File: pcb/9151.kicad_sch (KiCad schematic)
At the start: 22 parts, among them J1 SIM_Card, J10 Conn_01x02, J5 Conn_ARM_SWD_TagConnect_TC203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, J9 Conn_Coaxial, U1 nRF9151-LAXX, U3 W25Q128JVP

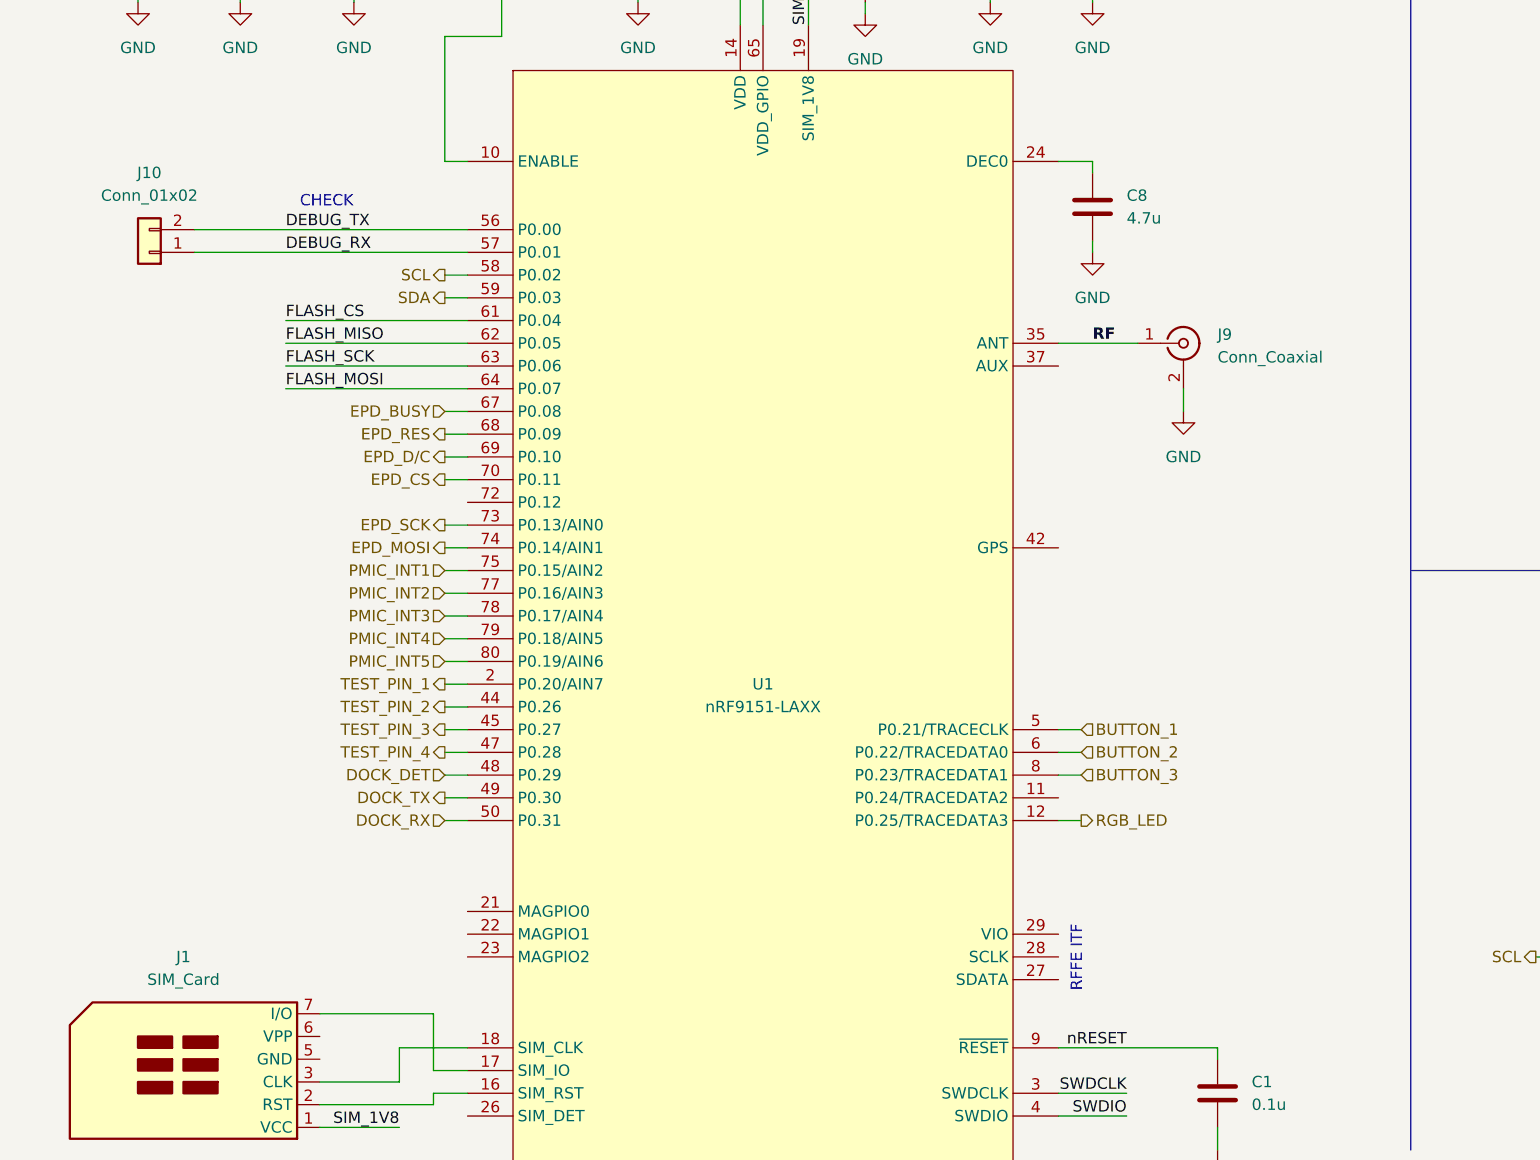
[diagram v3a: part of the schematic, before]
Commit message: Add netclasses and usb-to-uart
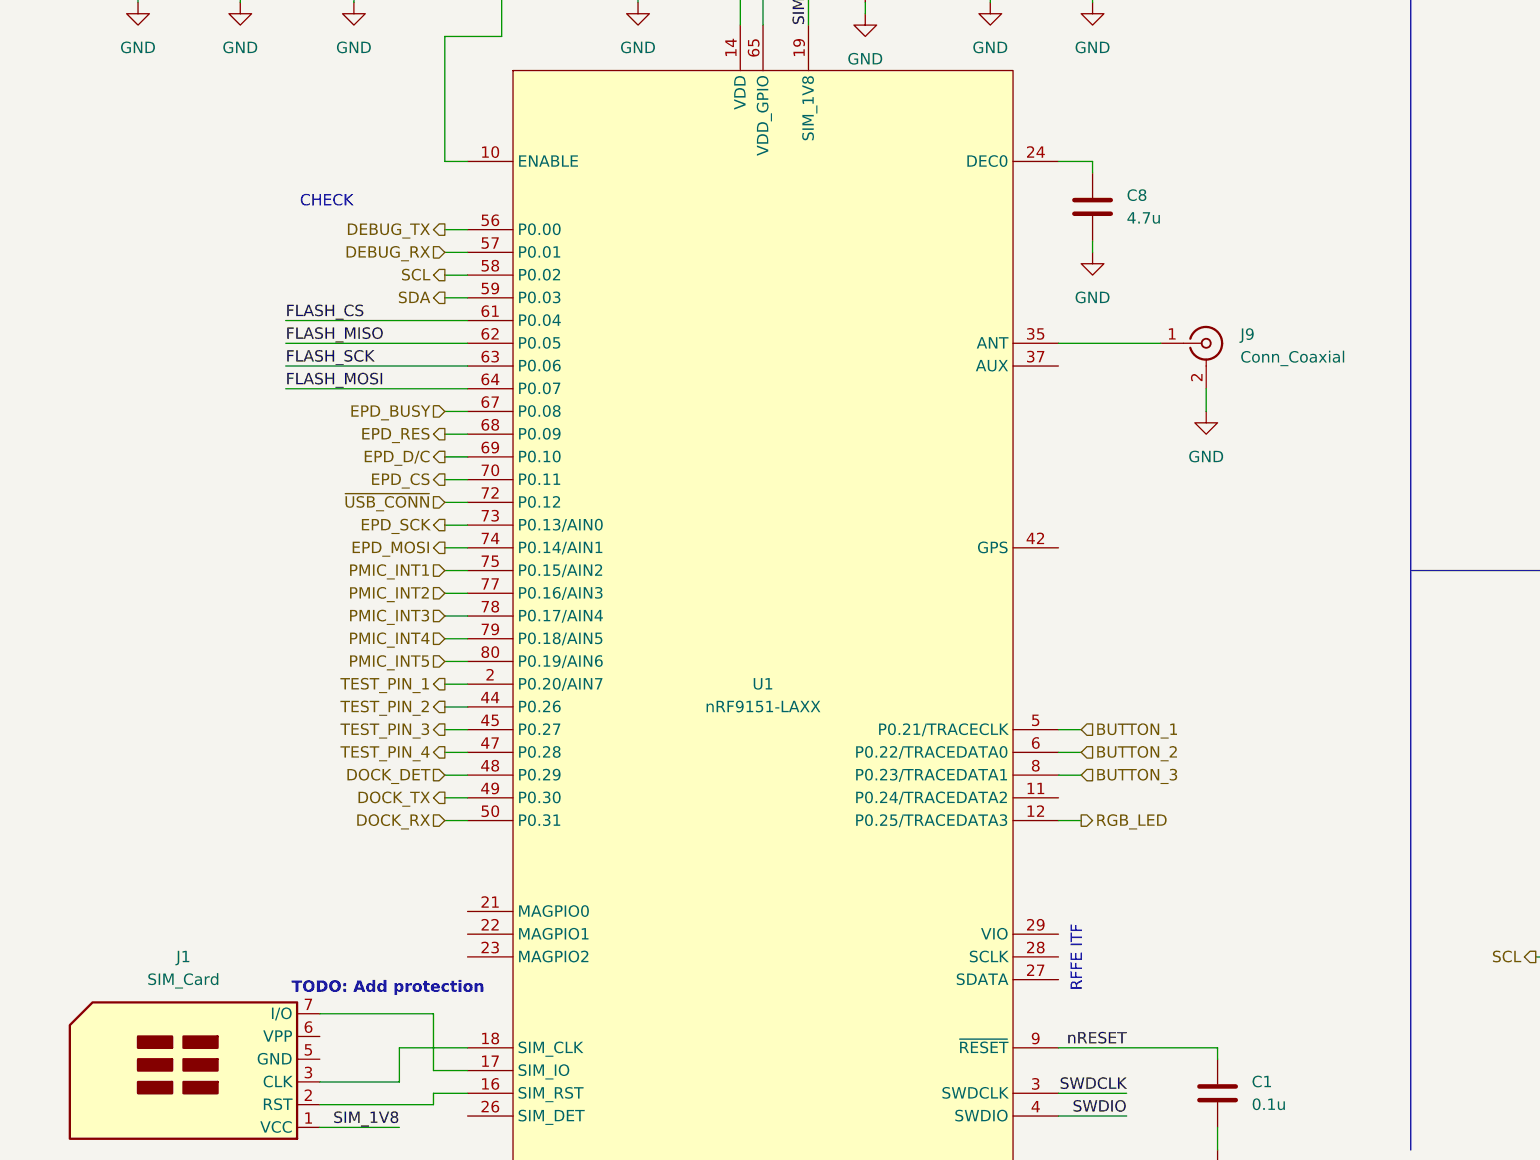
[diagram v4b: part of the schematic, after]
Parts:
- removed J10: Conn_01x02, symbol Connector_Generic:Conn_01x02
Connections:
- net ~{USB_CONN}: now reaches U1.72 (P0.12)
- net RF: no longer names the net of J9.1 (In), U1.35 (ANT)
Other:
- note added: "TODO: Add protection"
- moved on the sheet: J9
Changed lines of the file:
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@@
 		)
 	)
+	(text "TODO: Add protection"
+		(exclude_from_sim no)
+		(at 62.23 148.336 0)
+		(effects
+			(font
+				(size 1.27 1.27)
+				(thickness 0.254)
+				(bold yes)
+				(color 255 0 243 1)
+			)
+		)
+	)
 	(text "Internal pull-ups \nare good to 100kHz"
 		(exclude_from_sim no)
@@
 	(wire
 		(pts
+			(xy 68.58 63.5) (xy 71.12 63.5)
+		)
+		(stroke
+			(width 0)
+			(type default)
+		)
+	)
+	(wire
+		(pts
 			(xy 68.58 91.44) (xy 71.12 91.44)
 		)
@@
 	(wire
 		(pts
-			(xy 137.16 76.2) (xy 146.05 76.2)
+			(xy 137.16 76.2) (xy 148.59 76.2)
 		)
 		(stroke
@@
 	(wire
 		(pts
+			(xy 68.58 66.04) (xy 71.12 66.04)
+		)
+		(stroke
+			(width 0)
+			(type default)
+		)
+	)
+	(wire
+		(pts
 			(xy 254 54.61) (xy 254 57.15)
 		)
@@
 	(wire
 		(pts
+			(xy 68.58 93.98) (xy 71.12 93.98)
+		)
+		(stroke
+			(width 0)
+			(type default)
+		)
+	)
+	(wire
+		(pts
 			(xy 58.42 35.56) (xy 58.42 38.1)
 		)
@@
 	(wire
 		(pts
-			(xy 151.13 81.28) (xy 151.13 83.82)
+			(xy 153.67 81.28) (xy 153.67 83.82)
 		)
 		(stroke
@@
 	(wire
 		(pts
-			(xy 40.64 66.04) (xy 71.12 66.04)
-		)
-		(stroke
-			(width 0)
-			(type default)
-		)
-	)
-	(wire
-		(pts
-			(xy 40.64 63.5) (xy 71.12 63.5)
-		)
-		(stroke
-			(width 0)
-			(type default)
-		)
-	)
-	(wire
-		(pts
 			(xy 68.58 129.54) (xy 71.12 129.54)
 		)
@@
 		)
 	)
-	(label "DEBUG_TX"
-		(at 50.8 63.5 0)
-		(effects
-			(font
-				(size 1.27 1.27)
-			)
-			(justify left bottom)
-		)
-	)
 	(label "FLASH_CS"
 		(at 217.17 49.53 0)
@@
 		)
 	)
-	(label "RF"
-		(at 140.97 76.2 0)
-		(effects
-			(font
-				(size 1.27 1.27)
-				(thickness 0.254)
-				(bold yes)
-			)
-			(justify left bottom)
-		)
-	)
 	(label "SWDCLK"
 		(at 144.78 160.02 180)
@@
 		)
 	)
-	(label "DEBUG_RX"
-		(at 50.8 66.04 0)
-		(effects
-			(font
-				(size 1.27 1.27)
-			)
-			(justify left bottom)
-		)
-	)
 	(label "nRESET"
 		(at 144.78 154.94 180)
@@
 		)
 	)
+	(hierarchical_label "DEBUG_RX"
+		(shape input)
+		(at 68.58 66.04 180)
+		(effects
+			(font
+				(size 1.27 1.27)
+				(thickness 0.1588)
+			)
+			(justify right)
+		)
+	)
 	(hierarchical_label "EPD_D{slash}C"
 		(shape output)
@@
 		)
 	)
+	(hierarchical_label "~{USB_CONN}"
+		(shape input)
+		(at 68.58 93.98 180)
+		(effects
+			(font
+				(size 1.27 1.27)
+			)
+			(justify right)
+		)
+	)
 	(hierarchical_label "PMIC_INT4"
 		(shape input)
@@
 		)
 	)
+	(hierarchical_label "DEBUG_TX"
+		(shape output)
+		(at 68.58 63.5 180)
+		(effects
+			(font
+				(size 1.27 1.27)
+				(thickness 0.1588)
+			)
+			(justify right)
+		)
+	)
 	(hierarchical_label "EPD_BUSY"
 		(shape input)
@@
 		)
 	)
+	(netclass_flag ""
+		(length 2.54)
+		(shape round)
+		(at 78.74 26.67 0)
+		(fields_autoplaced yes)
+		(effects
+			(font
+				(size 1.27 1.27)
+			)
+			(justify left bottom)
+		)
+		(property "Netclass" "HIPOW"
+			(at 79.4385 24.13 0)
+			(effects
+				(font
+					(size 1.27 1.27)
+				)
+				(justify left)
+			)
+		)
+		(property "Component Class" ""
+			(at -85.09 5.08 0)
+			(effects
+				(font
+					(size 1.27 1.27)
+					(italic yes)
+				)
+			)
+		)
+	)
+	(netclass_flag ""
+		(length 2.54)
+		(shape round)
+		(at 138.43 76.2 0)
+		(fields_autoplaced yes)
+		(effects
+			(font
+				(size 1.27 1.27)
+			)
+			(justify left bottom)
+		)
+		(property "Netclass" "RF_50R"
+			(at 139.1285 73.66 0)
+			(effects
+				(font
+					(size 1.27 1.27)
+				)
+				(justify left)
+			)
+		)
+		(property "Component Class" ""
+			(at -17.78 1.27 0)
+			(effects
+				(font
+					(size 1.27 1.27)
+					(italic yes)
+				)
+			)
+		)
+	)
 	(symbol
 		(lib_id "Memory_Flash:W25Q128JVP")
@@
 	)
 	(symbol
-		(lib_id "Connector_Generic:Conn_01x02")
-		(at 35.56 66.04 180)
-		(unit 1)
-		(exclude_from_sim no)
-		(in_bom yes)
-		(on_board yes)
-		(dnp no)
-		(fields_autoplaced yes)
-		(property "Reference" "J10"
-			(at 35.56 57.15 0)
-			(effects
-				(font
-					(size 1.27 1.27)
-				)
-			)
-		)
-		(property "Value" "Conn_01x02"
-			(at 35.56 59.69 0)
-			(effects
-				(font
-					(size 1.27 1.27)
-				)
-			)
-		)
-		(property "Footprint" ""
-			(at 35.56 66.04 0)
-			(effects
-				(font
-					(size 1.27 1.27)
-				)
-				(hide yes)
-			)
-		)
-		(property "Datasheet" "~"
-			(at 35.56 66.04 0)
-			(effects
-				(font
-					(size 1.27 1.27)
-				)
-				(hide yes)
-			)
-		)
-		(property "Description" "Generic connector, single row, 01x02, script generated (kicad-library-utils/schlib/autogen/connector/)"
-			(at 35.56 66.04 0)
-			(effects
-				(font
-					(size 1.27 1.27)
-				)
-				(hide yes)
-			)
-		)
-		(pin "1"
-		)
-		(pin "2"
-		)
-		(instances
-			(project ""
-				(path "/e4766f3c-98ec-4040-9e57-7309e9dd2214/3c6e67a3-a459-411e-b958-c3a826ee49dc"
-					(reference "J10")
-					(unit 1)
-				)
-			)
-		)
-	)
-	(symbol
 		(lib_id "Device:R")
 		(at 207.01 46.99 0)
@@
 	(symbol
 		(lib_id "power:GND")
-		(at 151.13 83.82 0)
+		(at 153.67 83.82 0)
 		(unit 1)
 		(exclude_from_sim no)
@@
 		(fields_autoplaced yes)
 		(property "Reference" "#PWR08"
-			(at 151.13 90.17 0)
+			(at 153.67 90.17 0)
 			(effects
 				(font
@@
 		)
 		(property "Value" "GND"
-			(at 151.13 88.9 0)
+			(at 153.67 88.9 0)
 			(effects
 				(font
@@
 		)
 		(property "Footprint" ""
-			(at 151.13 83.82 0)
+			(at 153.67 83.82 0)
 			(effects
 				(font
@@
 		)
 		(property "Datasheet" ""
-			(at 151.13 83.82 0)
+			(at 153.67 83.82 0)
 			(effects
 				(font
@@
 		)
 		(property "Description" "Power symbol creates a global label with name \"GND\" , ground"
-			(at 151.13 83.82 0)
+			(at 153.67 83.82 0)
 			(effects
 				(font
@@
 	(symbol
 		(lib_id "Connector:Conn_Coaxial")
-		(at 151.13 76.2 0)
+		(at 153.67 76.2 0)
 		(unit 1)
 		(exclude_from_sim no)
@@
 		(fields_autoplaced yes)
 		(property "Reference" "J9"
-			(at 154.94 75.2231 0)
+			(at 157.48 75.2231 0)
 			(effects
 				(font
@@
 		)
 		(property "Value" "Conn_Coaxial"
-			(at 154.94 77.7631 0)
+			(at 157.48 77.7631 0)
 			(effects
 				(font
@@
 		)
 		(property "Footprint" "Connector_Coaxial:U.FL_Molex_MCRF_73412-0110_Vertical"
-			(at 151.13 76.2 0)
+			(at 153.67 76.2 0)
 			(effects
 				(font
@@
 		)
 		(property "Datasheet" "~"
-			(at 151.13 76.2 0)
+			(at 153.67 76.2 0)
 			(effects
 				(font
@@
 		)
 		(property "Description" "coaxial connector (BNC, SMA, SMB, SMC, Cinch/RCA, LEMO, ...)"
-			(at 151.13 76.2 0)
+			(at 153.67 76.2 0)
 			(effects
 				(font

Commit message: Adding filters
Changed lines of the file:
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@@
 	)
 	(hierarchical_label "SDA"
-		(shape output)
+		(shape bidirectional)
 		(at 68.58 71.12 180)
 		(effects

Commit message: Protection
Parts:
- removed J1: SIM_Card, Connector_Card:nanoSIM_GCT_SIM8060-6-0-14-00, symbol Connector:SIM_Card
- added J10: JAE_SIM_Card_SF72S006, Connector_JAE:JAE_SIM_Card_SF72S006, symbol Connector:JAE_SIM_Card_SF72S006
- added U4: TPD3F303DPV, Package_SON:Texas_R-PUSON-N8_USON-8-1EP_1.6x2.1mm_P0.5mm_EP0.4x1.7mm, symbol Power_Protection:TPD3F303DPV
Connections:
- net GND: now also J10.C5 (GND), J10.CSW, U4.9 (GND)
- net SIM_1V8: now also J10.C1 (VCC), U4.5 (V_{CC})
- net SIM_RST: now reaches U1.16 (SIM_RST)
- net SIM_RST: now also U4.8 (DATA1_IN)
- net SIM_IO: now reaches U1.17 (SIM_IO)
- net SIM_IO: now also U4.6 (DATA2_IN)
- net SIM_CLK: now reaches U1.18 (SIM_CLK)
- net SIM_CLK: now also U4.7 (CLK_IN)
- new net: J10.C2 (RST), U4.1 (DATA1_OUT)
- new net: J10.C3 (CLK), U4.2 (CLK_OUT)
- new net: J10.C7 (I/O), U4.3 (DATA2_OUT)
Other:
- note added: "SIM Card"
- note removed: "TODO: Add protection"
- moved on the sheet: C25, J5, R5, R6, R7, R8, U3
